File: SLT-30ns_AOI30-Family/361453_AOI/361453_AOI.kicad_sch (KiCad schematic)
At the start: 11 parts, among them T1 IBM_Transistor, U1 12-Pin_SLx_Can

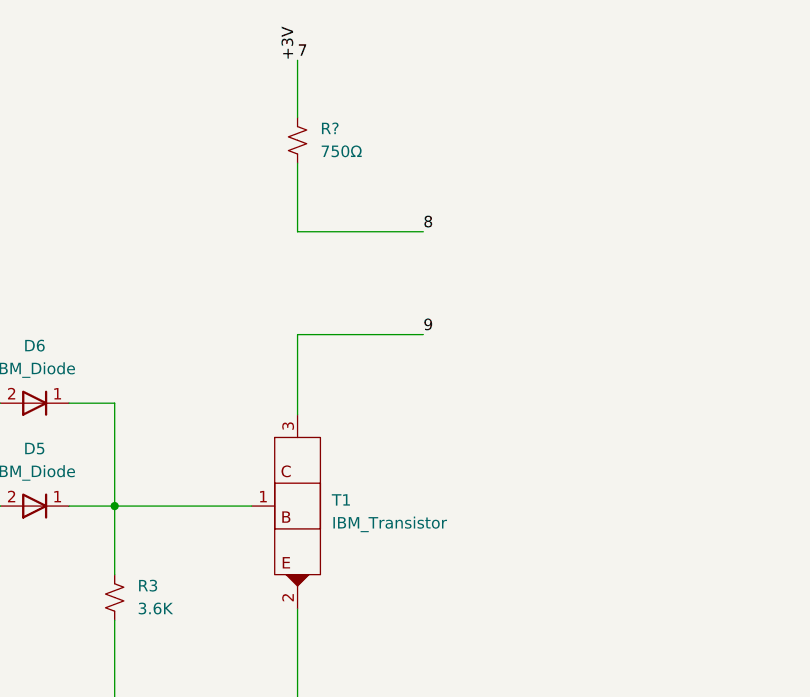
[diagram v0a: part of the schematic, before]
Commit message: Finished off the SLT-30 family of parts, started on the SLT-700 family. Changed labeling of transistors and diodes in all schematics, but have yet to update all the pdf files. This is a TODO...
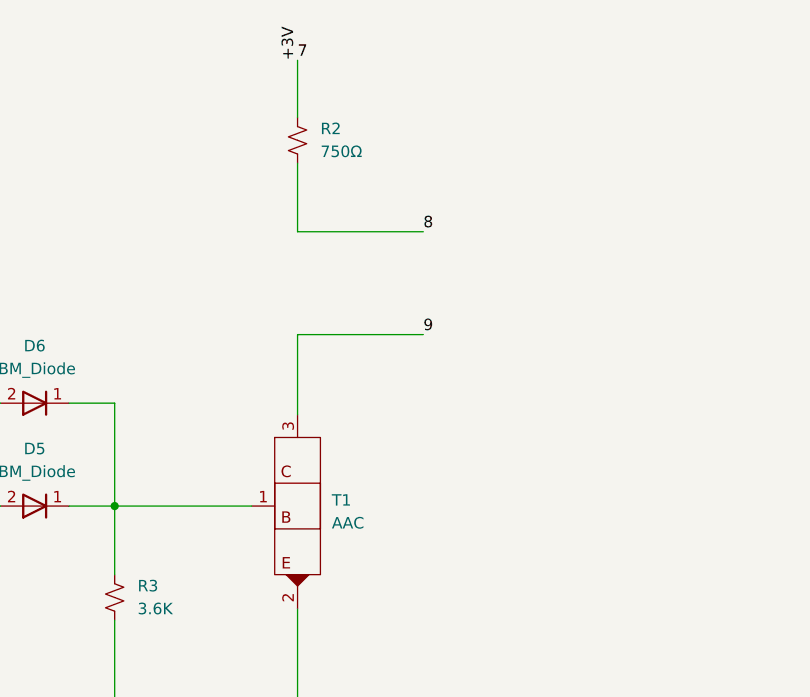
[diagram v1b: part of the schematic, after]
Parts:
- T1: value IBM_Transistor -> AAC
- gave numbers to parts that had none: 1
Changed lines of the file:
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@@
       (effects (font (size 1.27 1.27)) (justify left))
     )
-    (property "Value" "IBM_Transistor" (id 1) (at 160.02 95.8849 0)
+    (property "Value" "AAC" (id 1) (at 160.02 95.8849 0)
       (effects (font (size 1.27 1.27)) (justify left))
     )
@@
   (symbol (lib_id "Device:R_Small_US") (at 156.21 53.34 0) (unit 1)
     (in_bom yes) (on_board yes) (fields_autoplaced)
-    (property "Reference" "R?" (id 0) (at 158.75 52.0699 0)
+    (property "Reference" "R2" (id 0) (at 158.75 52.0699 0)
       (effects (font (size 1.27 1.27)) (justify left))
     )
@@
       (reference "R1") (unit 1) (value "2K") (footprint "Resistor_SMD:R_0201_0603Metric")
     )
+    (path "/94dd523f-5529-4374-bb00-a68226b4e5f7"
+      (reference "R2") (unit 1) (value "750Ω") (footprint "Resistor_SMD:R_0201_0603Metric")
+    )
     (path "/e3b34507-97c6-4732-8351-5f7d2bda9963"
       (reference "R3") (unit 1) (value "3.6K") (footprint "Resistor_SMD:R_0201_0603Metric")
     )
-    (path "/94dd523f-5529-4374-bb00-a68226b4e5f7"
-      (reference "R?") (unit 1) (value "750Ω") (footprint "Resistor_SMD:R_0201_0603Metric")
-    )
     (path "/848b9538-2d58-4033-a17d-c5449fb2184a"
-      (reference "T1") (unit 1) (value "IBM_Transistor") (footprint "")
+      (reference "T1") (unit 1) (value "AAC") (footprint "")
     )
     (path "/75e072b9-86c1-407b-a1c4-16b7a7044004"

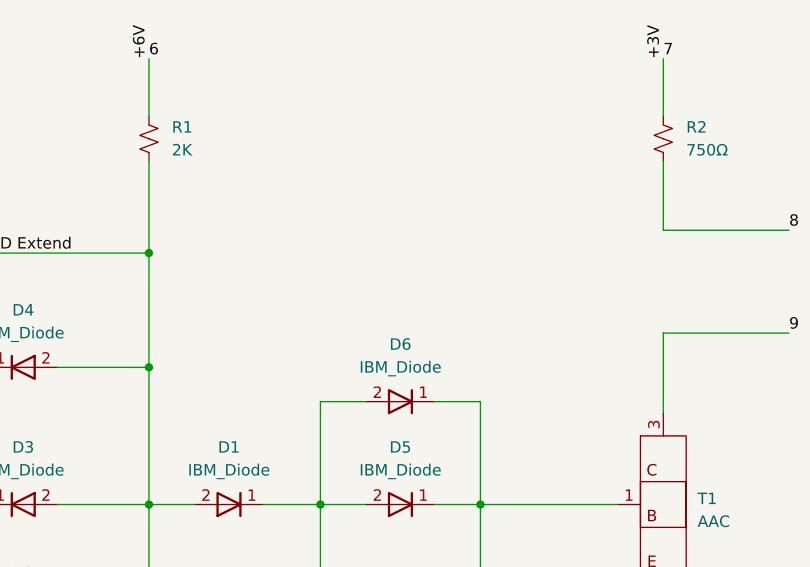
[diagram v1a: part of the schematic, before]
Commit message: Update schematic pdfs
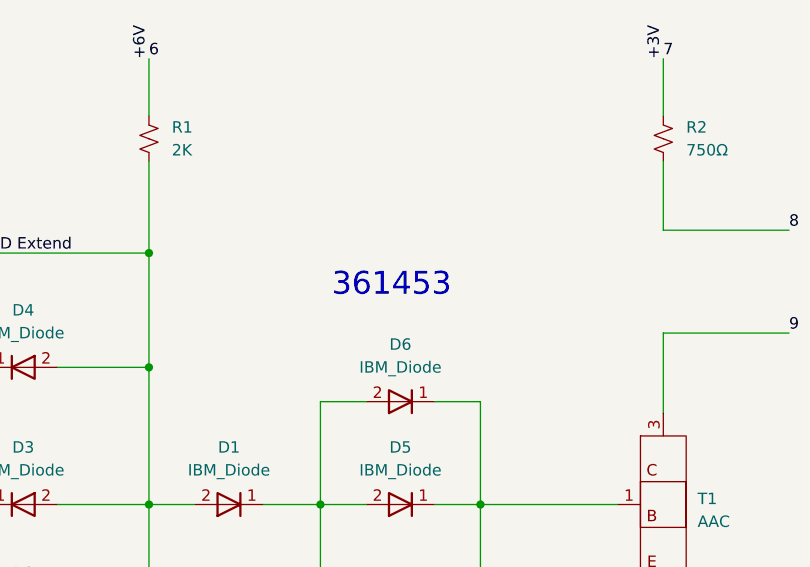
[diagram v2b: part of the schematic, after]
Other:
- note added: "361453"
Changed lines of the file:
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@@
     (stroke (width 0) (type default) (color 0 0 0 0))
+  )
+  (text "361453" (at 119.38 71.12 0)
+    (effects (font (size 2.54 2.54)) (justify left bottom))
   )
   (label "8" (at 170.18 63.5 0)
